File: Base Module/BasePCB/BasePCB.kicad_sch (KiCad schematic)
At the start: 140 parts, among them J1 USB_A, SW1 SW_Push, U1 ATmega32U4-A, Y1 Crystal_GND24_Small

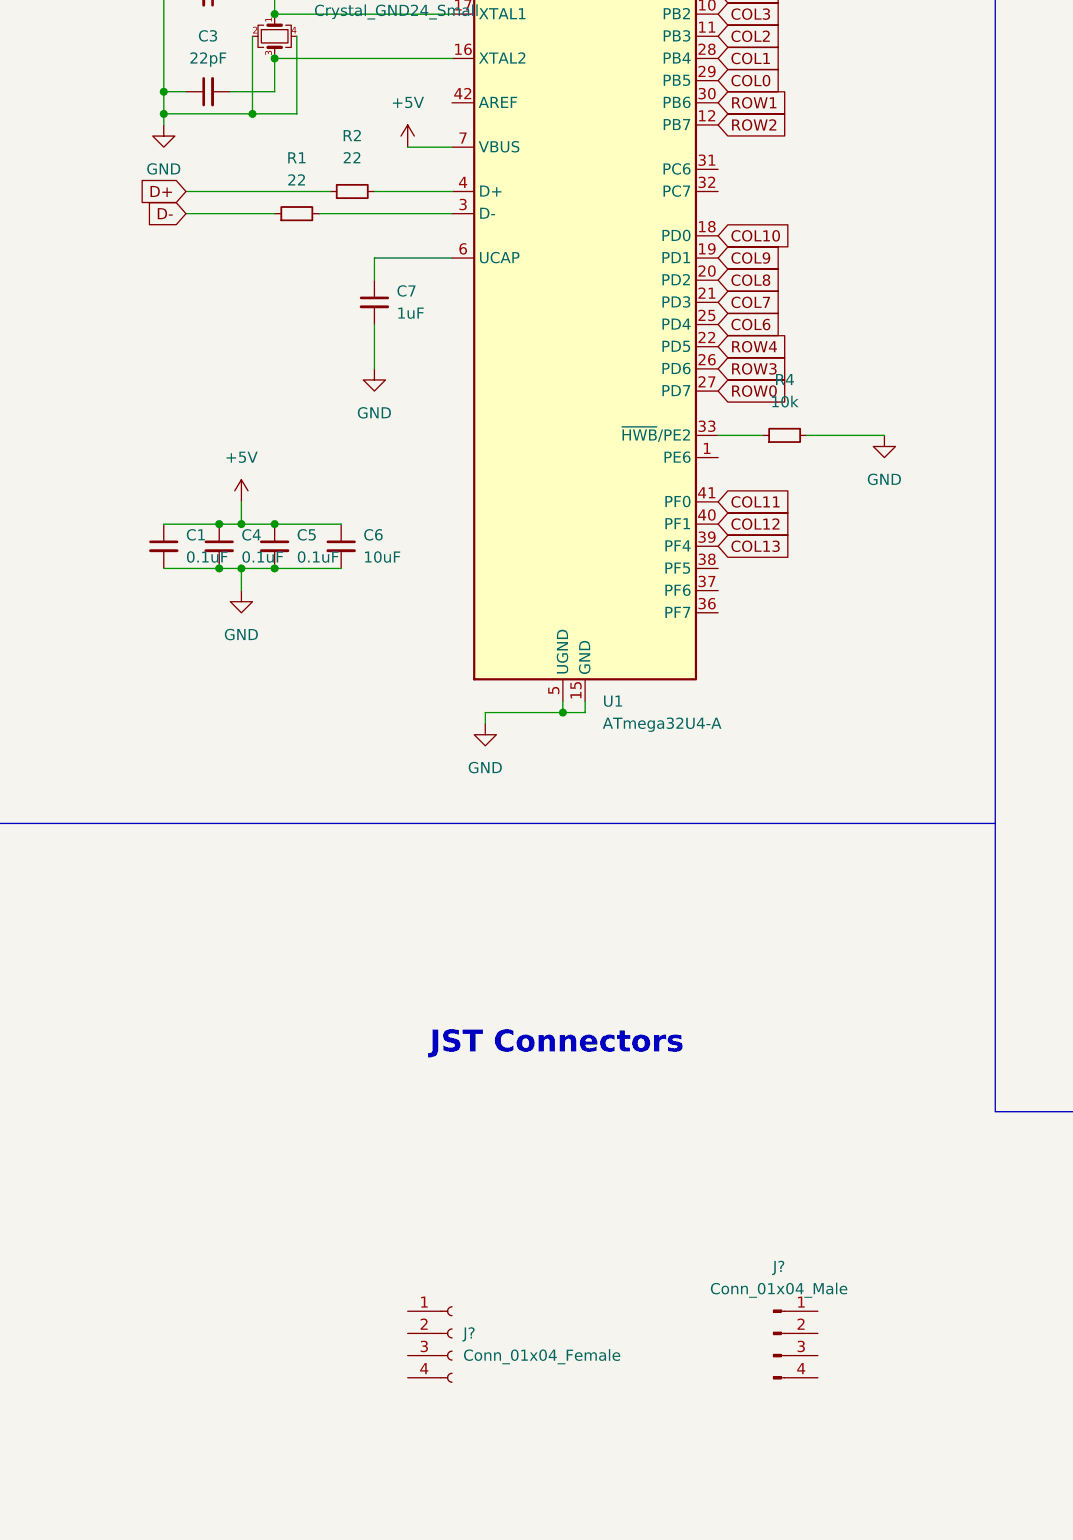
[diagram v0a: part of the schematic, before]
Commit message: Updated connectors, annotated schematic
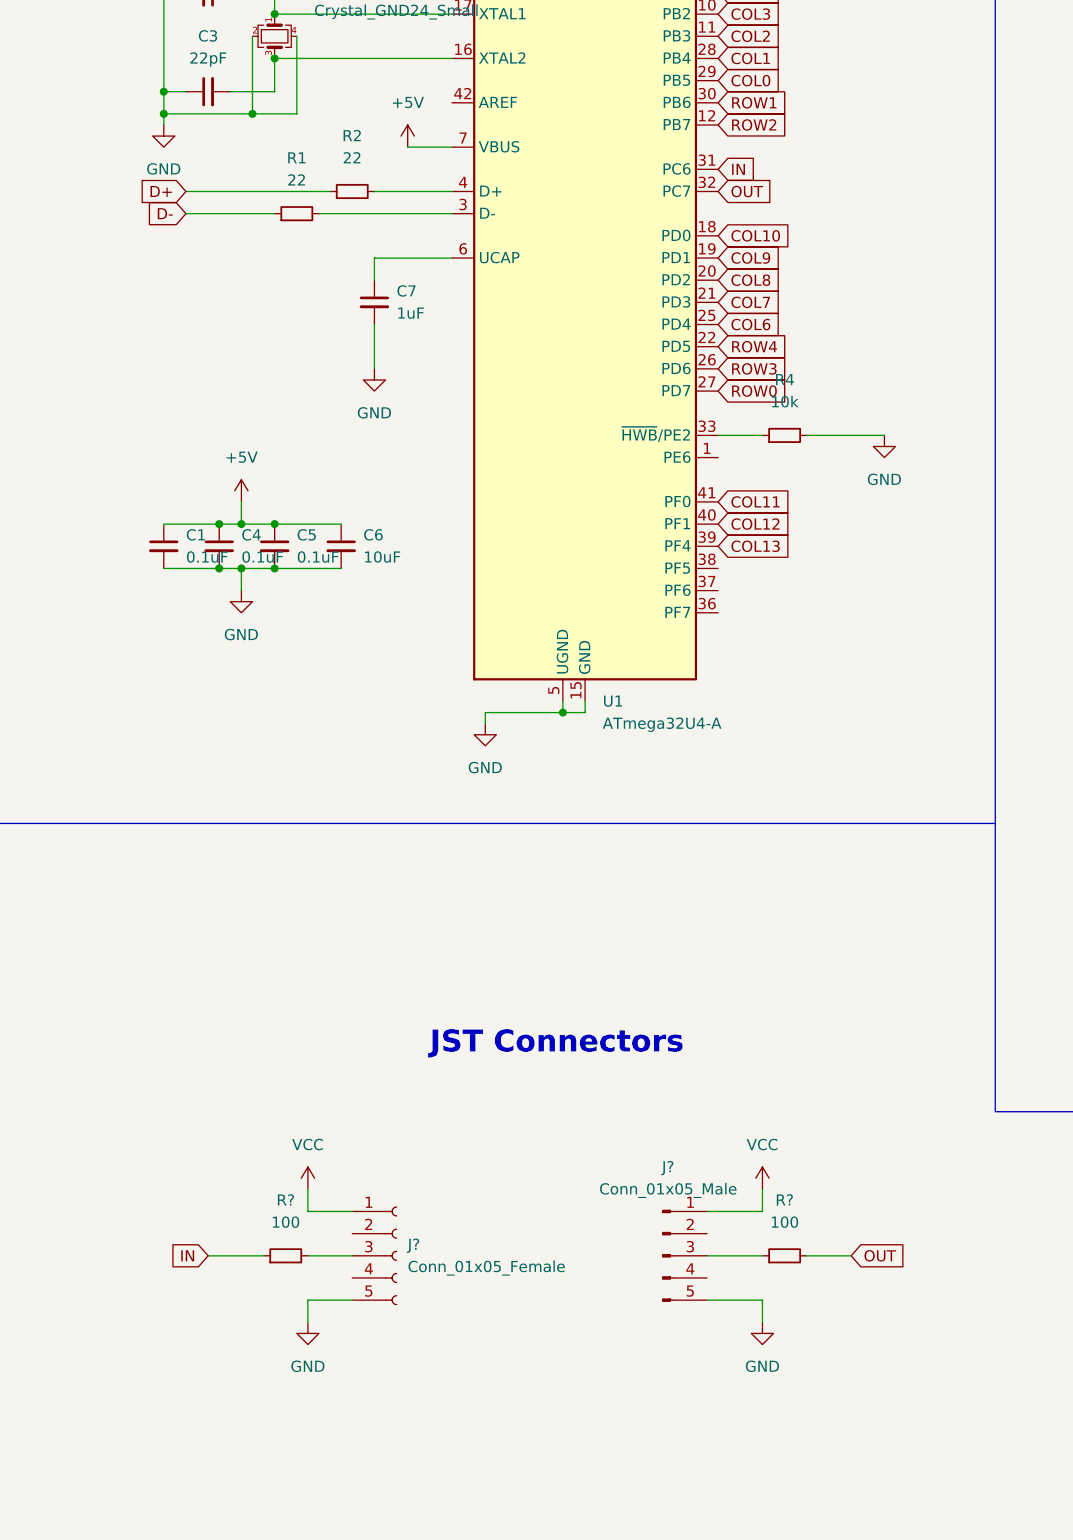
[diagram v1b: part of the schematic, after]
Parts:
- removed J?: Conn_01x04_Female, symbol Connector:Conn_01x04_Female
- removed J?: Conn_01x04_Male, symbol Connector:Conn_01x04_Male
- added J?: Conn_01x05_Male, symbol Connector:Conn_01x05_Male
- added J?: Conn_01x05_Female, symbol Connector:Conn_01x05_Female
- added R? (x2): 100, symbol Device:R_Small
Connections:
- net GND: now also J?.5 (Pin_5), J?.5 (Pin_5)
- net VCC: now also J?.1 (Pin_1), J?.1 (Pin_1)
- net IN: now reaches U1.31 (PC6)
- net IN: now also R?.1
- net OUT: now reaches U1.32 (PC7)
- net OUT: now also R?.2
- new net: J?.3 (Pin_3), R?.1
- new net: J?.3 (Pin_3), R?.2

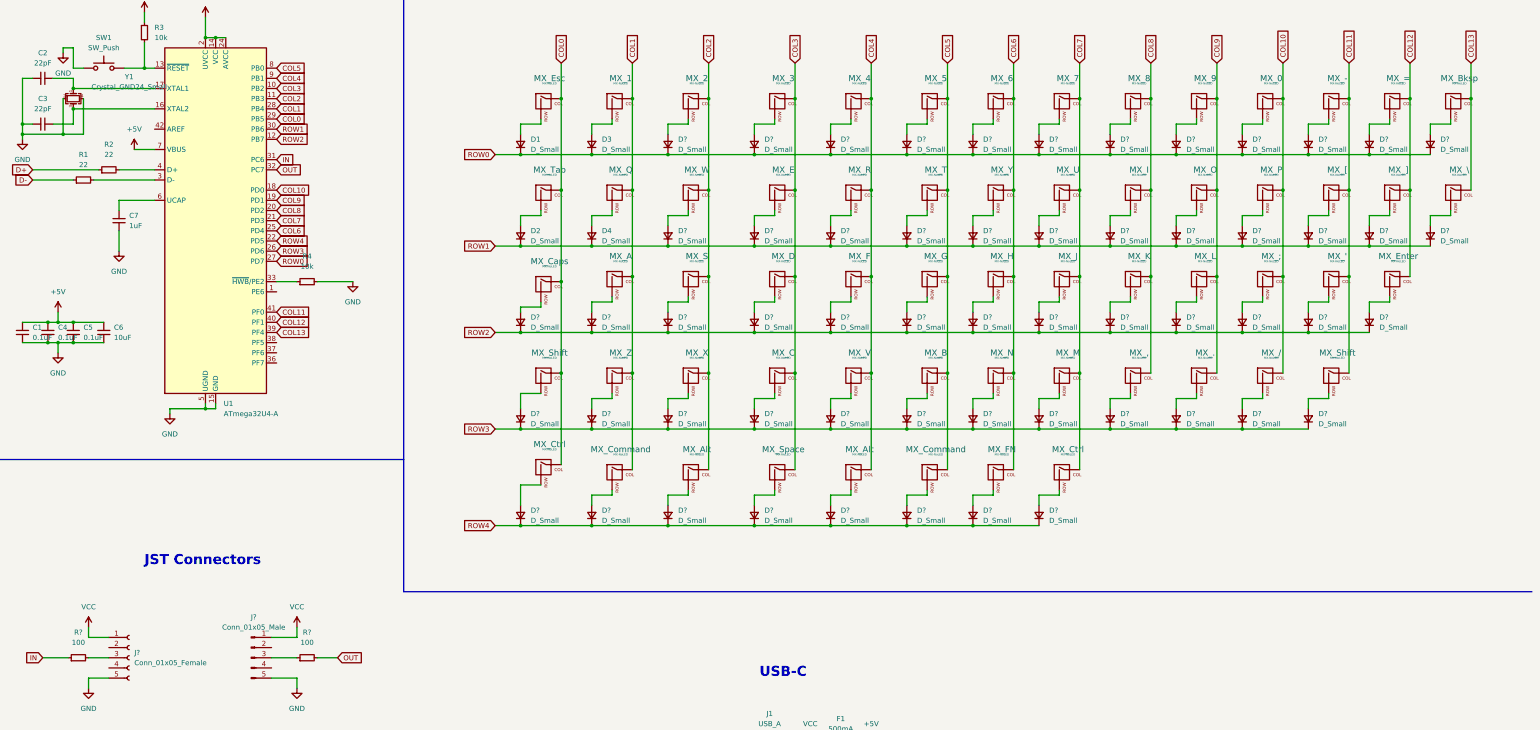
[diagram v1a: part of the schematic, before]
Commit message: Assigned remaining footprints
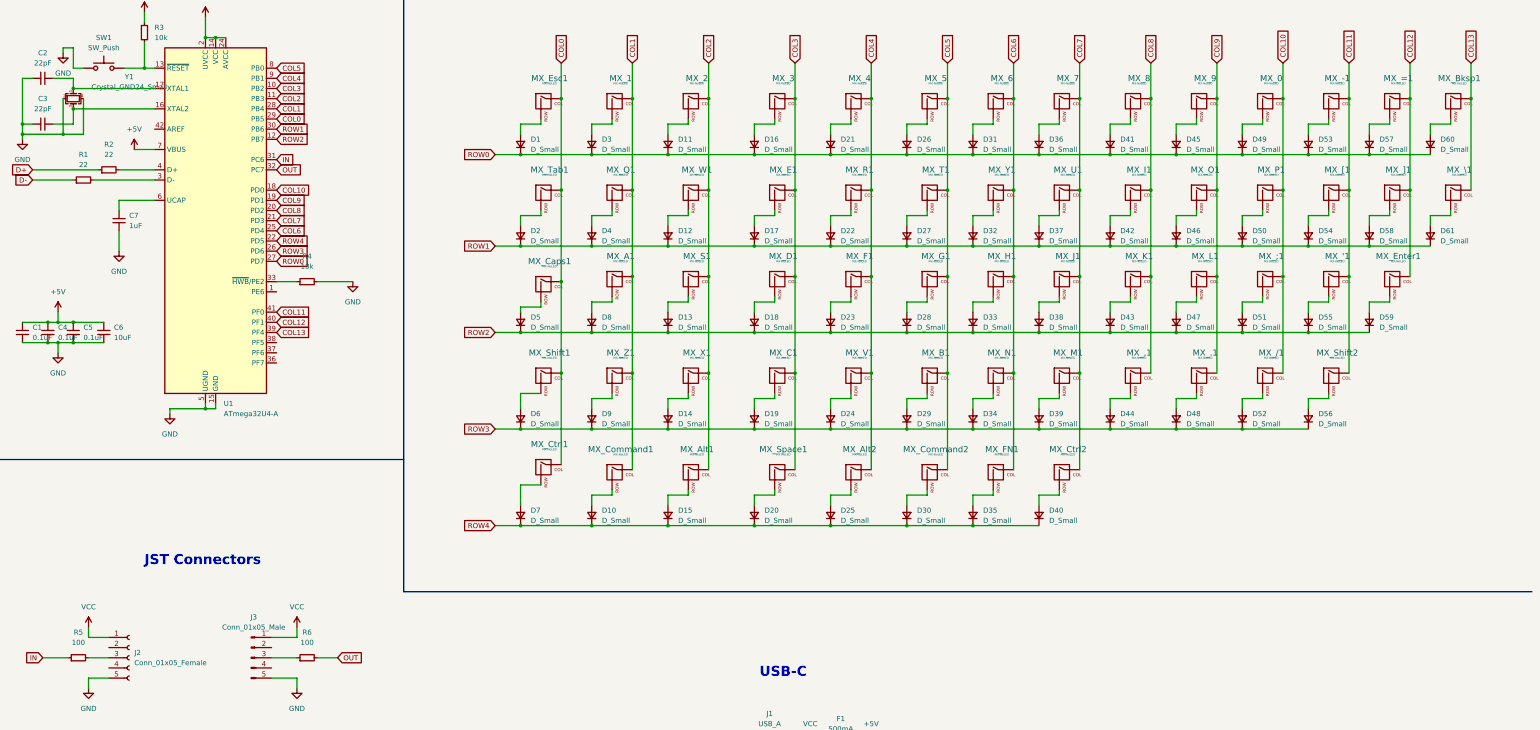
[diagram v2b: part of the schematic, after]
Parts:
- J2, J3: renamed from J?; footprint (none) -> Connector_JST:JST_PH_S5B-PH-K_1x05_P2.00mm_Horizontal
- R5, R6: renamed from R?; footprint (none) -> Resistor_SMD:R_0805_2012Metric
- gave numbers to parts that had none: 57
- renumbered MX_' to MX_'1, MX_, to MX_,1, MX_- to MX_-1, MX_. to MX_.1, MX_/ to MX_/1, MX_; to MX_;1, MX_= to MX_=1, MX_A to MX_A1, MX_Alt to MX_Alt1, MX_Alt to MX_Alt2, MX_B to MX_B1, MX_Bksp to MX_Bksp1, MX_C to MX_C1, MX_Caps to MX_Caps1, MX_Command to MX_Command1, MX_Command to MX_Command2, MX_Ctrl to MX_Ctrl1, MX_Ctrl to MX_Ctrl2, MX_D to MX_D1, MX_E to MX_E1, MX_Enter to MX_Enter1, MX_Esc to MX_Esc1, MX_F to MX_F1, MX_FN to MX_FN1, MX_G to MX_G1, MX_H to MX_H1, MX_I to MX_I1, MX_J to MX_J1, MX_K to MX_K1, MX_L to MX_L1, MX_M to MX_M1, MX_N to MX_N1, MX_O to MX_O1, MX_P to MX_P1, MX_Q to MX_Q1, MX_R to MX_R1, MX_S to MX_S1, MX_Shift to MX_Shift1, MX_Shift to MX_Shift2, MX_Space to MX_Space1, MX_T to MX_T1, MX_Tab to MX_Tab1, MX_U to MX_U1, MX_V to MX_V1, MX_W to MX_W1, MX_X to MX_X1, MX_Y to MX_Y1, MX_Z to MX_Z1, MX_[ to MX_[1, MX_\ to MX_\1, MX_] to MX_]1

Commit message: Updated schematic
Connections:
- net IN: now also R6.2; no longer R5.1
- net OUT: now also R5.1; no longer R6.2
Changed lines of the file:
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@@
     )
   )
-  (global_label "IN" (shape input) (at 36.83 205.74 180) (fields_autoplaced)
-    (effects (font (size 1.27 1.27)) (justify right))
-    (property "Intersheet References" "${INTERSHEET_REFS}" (id 0) (at 32.4817 205.6606 0)
+  (global_label "OUT" (shape input) (at 36.83 205.74 180) (fields_autoplaced)
+    (effects (font (size 1.27 1.27)) (justify right))
+    (property "Intersheet References" "${INTERSHEET_REFS}" (id 0) (at 30.7883 205.6606 0)
       (effects (font (size 1.27 1.27)) (justify right) hide)
     )
@@
     )
   )
-  (global_label "OUT" (shape input) (at 110.49 205.74 0) (fields_autoplaced)
-    (effects (font (size 1.27 1.27)) (justify left))
-    (property "Intersheet References" "${INTERSHEET_REFS}" (id 0) (at 116.5317 205.6606 0)
-      (effects (font (size 1.27 1.27)) (justify left) hide)
-    )
+  (global_label "IN" (shape input) (at 110.49 205.74 0) (fields_autoplaced)
+    (effects (font (size 1.27 1.27)) (justify left))
+    (property "Intersheet References" "${INTERSHEET_REFS}" (id 0) (at 114.8383 205.6606 0)
+      (effects (font (size 1.27 1.27)) (justify left) hide)
+    )

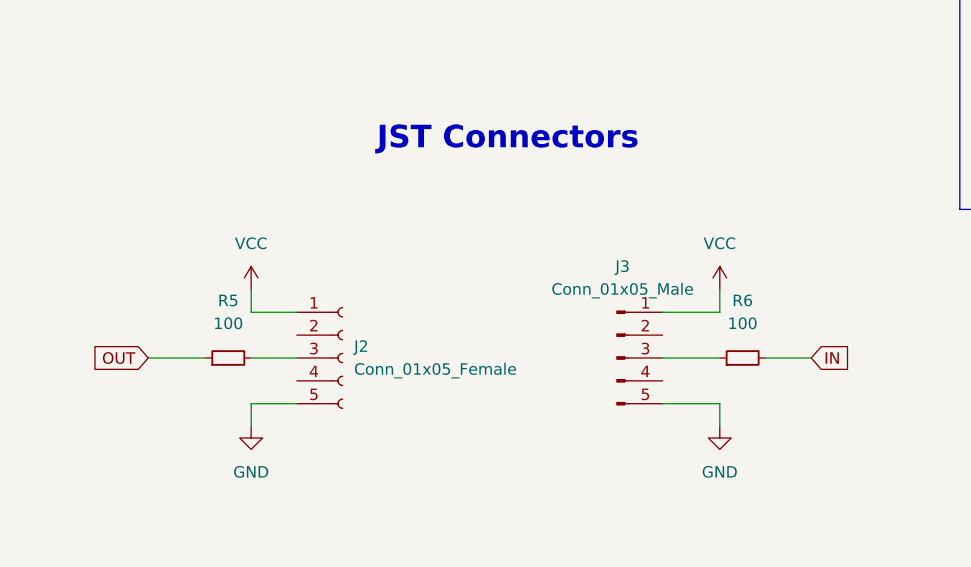
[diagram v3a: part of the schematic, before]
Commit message: Updated connectors
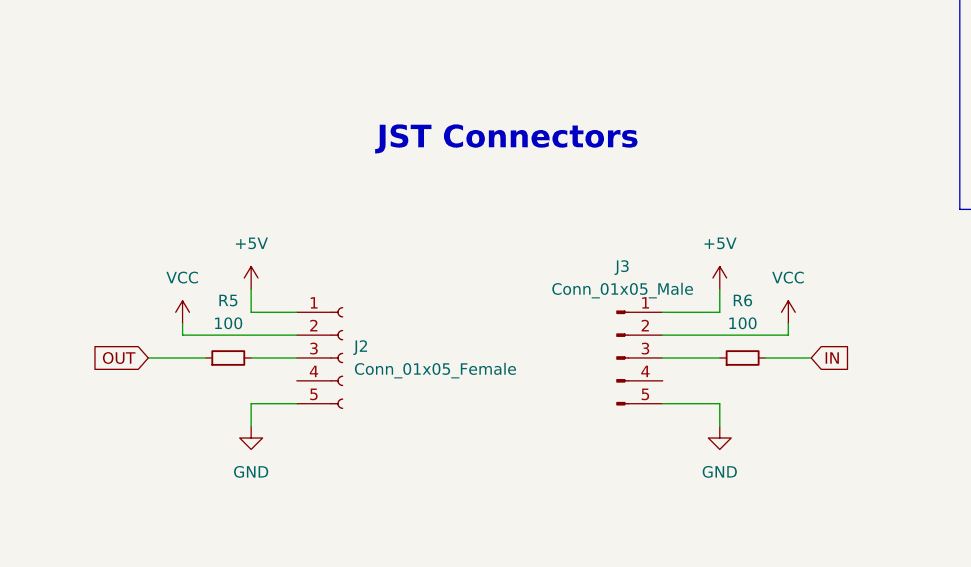
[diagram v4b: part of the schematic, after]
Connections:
- net +5V: now also J2.1 (Pin_1), J3.1 (Pin_1)
- net VCC: now also J2.2 (Pin_2), J3.2 (Pin_2); no longer J2.1 (Pin_1), J3.1 (Pin_1)
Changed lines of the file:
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@@
     (stroke (width 0) (type default) (color 0 0 0 0))
   )
+  (wire (pts (xy 40.64 203.2) (xy 53.34 203.2))
+    (stroke (width 0) (type default) (color 0 0 0 0))
+  )
   (wire (pts (xy 285.75 143.51) (xy 285.75 140.97))
     (stroke (width 0) (type default) (color 0 0 0 0))
@@
     (stroke (width 0) (type default) (color 0 0 0 0))
   )
+  (wire (pts (xy 107.95 201.93) (xy 107.95 203.2))
+    (stroke (width 0) (type default) (color 0 0 0 0))
+  )
   (wire (pts (xy 214.63 119.38) (xy 214.63 116.84))
     (stroke (width 0) (type default) (color 0 0 0 0))
@@
     (stroke (width 0) (type default) (color 0 0 0 0))
   )
+  (wire (pts (xy 40.64 201.93) (xy 40.64 203.2))
+    (stroke (width 0) (type default) (color 0 0 0 0))
+  )
   (wire (pts (xy 156.21 124.46) (xy 173.99 124.46))
     (stroke (width 0) (type default) (color 0 0 0 0))
@@
     (stroke (width 0) (type default) (color 0 0 0 0))
   )
+  (wire (pts (xy 107.95 203.2) (xy 93.98 203.2))
+    (stroke (width 0) (type default) (color 0 0 0 0))
+  )
   (wire (pts (xy 173.99 74.93) (xy 173.99 72.39))
     (stroke (width 0) (type default) (color 0 0 0 0))
@@
     (pin "2")
   )
+  (symbol (lib_id "power:+5V") (at 100.33 198.12 0) (unit 1)
+    (in_bom yes) (on_board yes) (fields_autoplaced)
+    (property "Reference" "#PWR?" (id 0) (at 100.33 201.93 0)
+      (effects (font (size 1.27 1.27)) hide)
+    )
+    (property "Value" "+5V" (id 1) (at 100.33 193.04 0))
+    (property "Footprint" "" (id 2) (at 100.33 198.12 0)
+      (effects (font (size 1.27 1.27)) hide)
+    )
+    (property "Datasheet" "" (id 3) (at 100.33 198.12 0)
+      (effects (font (size 1.27 1.27)) hide)
+    )
+    (pin "1")
+  )
   (symbol (lib_id "MX_Alps_Hybrid:MX-NoLED") (at 359.41 135.89 0) (unit 1)
     (in_bom yes) (on_board yes) (fields_autoplaced)
@@
     (pin "2")
   )
-  (symbol (lib_id "power:VCC") (at 100.33 198.12 0) (unit 1)
+  (symbol (lib_id "power:VCC") (at 107.95 201.93 0) (unit 1)
     (in_bom yes) (on_board yes) (fields_autoplaced)
-    (property "Reference" "#PWR0115" (id 0) (at 100.33 201.93 0)
+    (property "Reference" "#PWR0115" (id 0) (at 107.95 205.74 0)
       (effects (font (size 1.27 1.27)) hide)
     )
-    (property "Value" "VCC" (id 1) (at 100.33 193.04 0))
-    (property "Footprint" "" (id 2) (at 100.33 198.12 0)
+    (property "Value" "VCC" (id 1) (at 107.95 196.85 0))
+    (property "Footprint" "" (id 2) (at 107.95 201.93 0)
       (effects (font (size 1.27 1.27)) hide)
     )
-    (property "Datasheet" "" (id 3) (at 100.33 198.12 0)
+    (property "Datasheet" "" (id 3) (at 107.95 201.93 0)
       (effects (font (size 1.27 1.27)) hide)
     )
@@
     (pin "2")
   )
-  (symbol (lib_id "power:VCC") (at 48.26 198.12 0) (unit 1)
+  (symbol (lib_id "power:VCC") (at 40.64 201.93 0) (unit 1)
     (in_bom yes) (on_board yes) (fields_autoplaced)
-    (property "Reference" "#PWR0114" (id 0) (at 48.26 201.93 0)
+    (property "Reference" "#PWR0114" (id 0) (at 40.64 205.74 0)
       (effects (font (size 1.27 1.27)) hide)
     )
-    (property "Value" "VCC" (id 1) (at 48.26 193.04 0))
-    (property "Footprint" "" (id 2) (at 48.26 198.12 0)
+    (property "Value" "VCC" (id 1) (at 40.64 196.85 0))
+    (property "Footprint" "" (id 2) (at 40.64 201.93 0)
       (effects (font (size 1.27 1.27)) hide)
     )
-    (property "Datasheet" "" (id 3) (at 48.26 198.12 0)
+    (property "Datasheet" "" (id 3) (at 40.64 201.93 0)
       (effects (font (size 1.27 1.27)) hide)
     )
@@
     (pin "2")
   )
+  (symbol (lib_id "power:+5V") (at 48.26 198.12 0) (unit 1)
+    (in_bom yes) (on_board yes) (fields_autoplaced)
+    (property "Reference" "#PWR?" (id 0) (at 48.26 201.93 0)
+      (effects (font (size 1.27 1.27)) hide)
+    )
+    (property "Value" "+5V" (id 1) (at 48.26 193.04 0))
+    (property "Footprint" "" (id 2) (at 48.26 198.12 0)
+      (effects (font (size 1.27 1.27)) hide)
+    )
+    (property "Datasheet" "" (id 3) (at 48.26 198.12 0)
+      (effects (font (size 1.27 1.27)) hide)
+    )
+    (pin "1")
+  )
   (symbol (lib_id "Device:D_Small") (at 303.53 100.33 90) (unit 1)
     (in_bom yes) (on_board yes) (fields_autoplaced)
@@
       (reference "#PWR0117") (unit 1) (value "GND") (footprint "")
     )
+    (path "/25c9cf7e-8afb-4388-b018-b0aabaa281ea"
+      (reference "#PWR?") (unit 1) (value "+5V") (footprint "")
+    )
+    (path "/c2e35ef1-adb4-4087-b819-4dfb86c3d2d4"
+      (reference "#PWR?") (unit 1) (value "+5V") (footprint "")
+    )
     (path "/af2d8d3e-eb34-45df-b58c-071efde6f073"
